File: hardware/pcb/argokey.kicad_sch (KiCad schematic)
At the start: 177 parts, among them J1 USB_BOOT, J2 GPIO, J3 Screen, J4 Debug, J5 USB_C_Receptacle_USB2.0, SW1 RotaryEncoder_Switch, SW2 RESET, U1 W25Q128JVS, U2 RP2040, U3 NCP1117-3.3_SOT223, Y1 ABLS-12.000MHZ-B4-T

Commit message: "Sch: Assign most footprints"
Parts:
- C1, C10, C11, C12, C13, C14, C16, C17, C19, C2, C3, C4, C5, C6, C7, C8, C9: footprint (none) -> Capacitor_SMD:C_0402_1005Metric_Pad0.74x0.62mm_HandSolder
- C15, C18: footprint (none) -> Capacitor_SMD:C_0805_2012Metric_Pad1.18x1.45mm_HandSolder
- D1, D10, D11, D12, D13, D14, D15, D16, D17, D18, D19, D2, D20, D21, D22, D23, D24, D25, D26, D27, D28, D29, D3, D30, D31, D32, D33, D34, D35, D36, D37, D38, D39, D4, D40, D41, D42, D43, D44, D45, D46, D47, D48, D49, D5, D50, D51, D52, D53, D54, D55, D56, D57, D58, D59, D6, D60, D61, D62, D63, D64, D65, D66, D67, D68, D69, D7, D8, D9: footprint (none) -> Diode_SMD:D_SOD-123
- J1: footprint (none) -> Connector_PinHeader_2.54mm:PinHeader_1x02_P2.54mm_Vertical
- J2: footprint (none) -> Connector_PinHeader_2.54mm:PinHeader_1x12_P2.54mm_Horizontal
- J3: footprint (none) -> Connector_PinHeader_2.54mm:PinHeader_1x04_P2.54mm_Vertical
- J4: footprint (none) -> Connector_PinHeader_2.54mm:PinHeader_1x04_P2.54mm_Horizontal
- R1, R10, R2, R3, R4, R5, R6, R7, R8, R9: footprint (none) -> Resistor_SMD:R_0402_1005Metric_Pad0.72x0.64mm_HandSolder
- S1, S10, S11, S12, S14, S15, S16, S17, S19, S20, S21, S22, S24, S25, S26, S27, S29, S30, S31, S32, S33, S34, S35, S36, S37, S38, S39, S40, S41, S42, S43, S44, S45, S46, S47, S48, S49, S5, S50, S51, S52, S53, S54, S55, S56, S58, S59, S6, S60, S62, S63, S66, S67, S68, S7, S8, S9: footprint (none) -> Button_Switch_Keyboard:SW_Cherry_MX_1.00u_PCB
- S13, S18, S23: footprint (none) -> Button_Switch_Keyboard:SW_Cherry_MX_1.25u_PCB
- S2, S65: footprint (none) -> Button_Switch_Keyboard:SW_Cherry_MX_1.50u_PCB
- S28: footprint (none) -> Button_Switch_Keyboard:SW_Cherry_MX_6.25u_PCB
- S3, S57: footprint (none) -> Button_Switch_Keyboard:SW_Cherry_MX_1.75u_PCB
- S4, S61: footprint (none) -> Button_Switch_Keyboard:SW_Cherry_MX_2.25u_PCB
- S64: footprint (none) -> Button_Switch_Keyboard:SW_Cherry_MX_2.00u_PCB
- U2: footprint IC57_RP2040 -> RP2040:RP2040

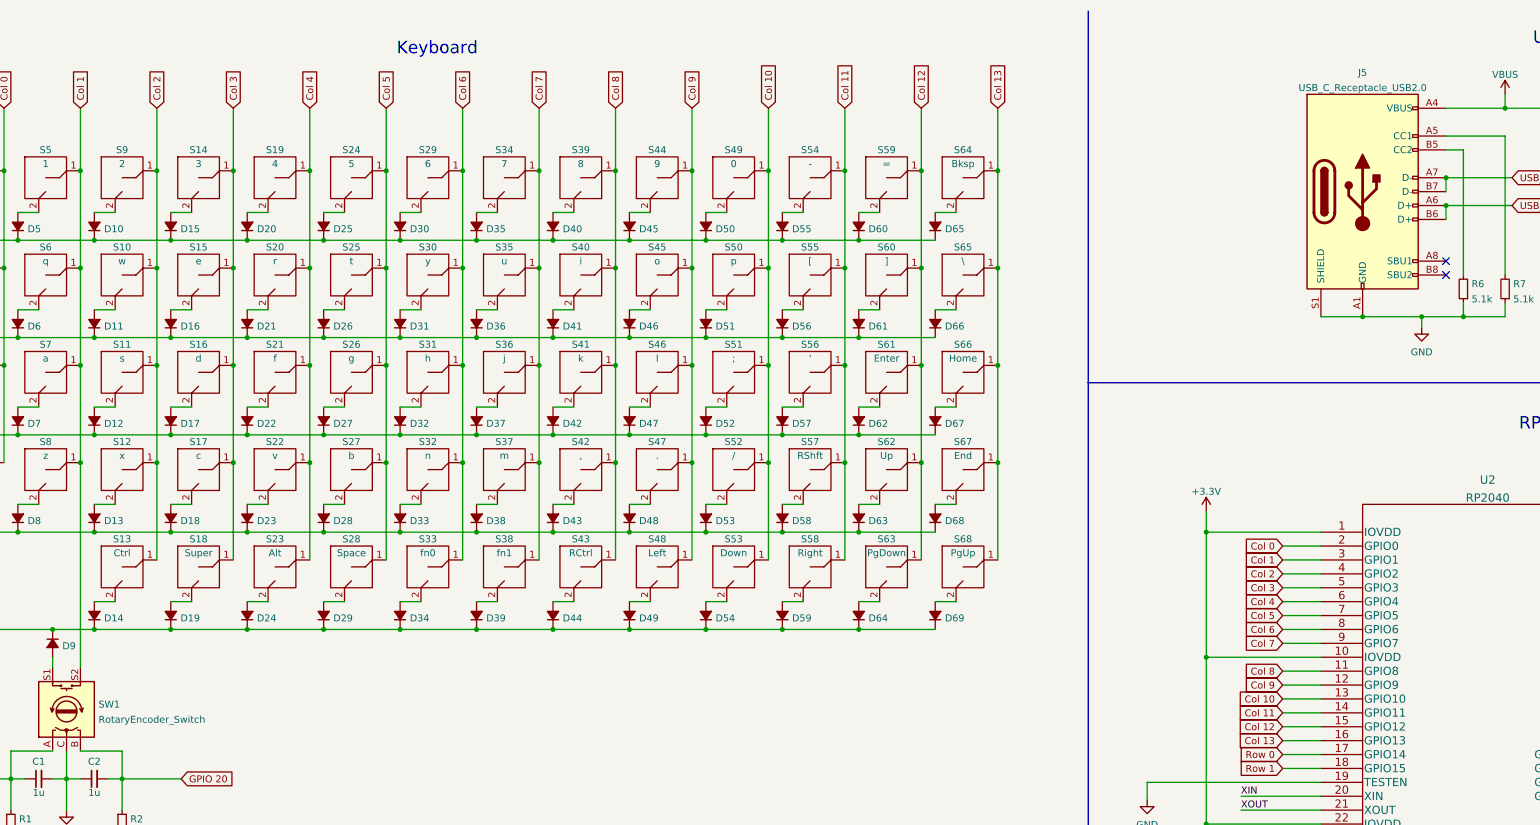
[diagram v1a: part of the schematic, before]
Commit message: Sch: Remove Diode values
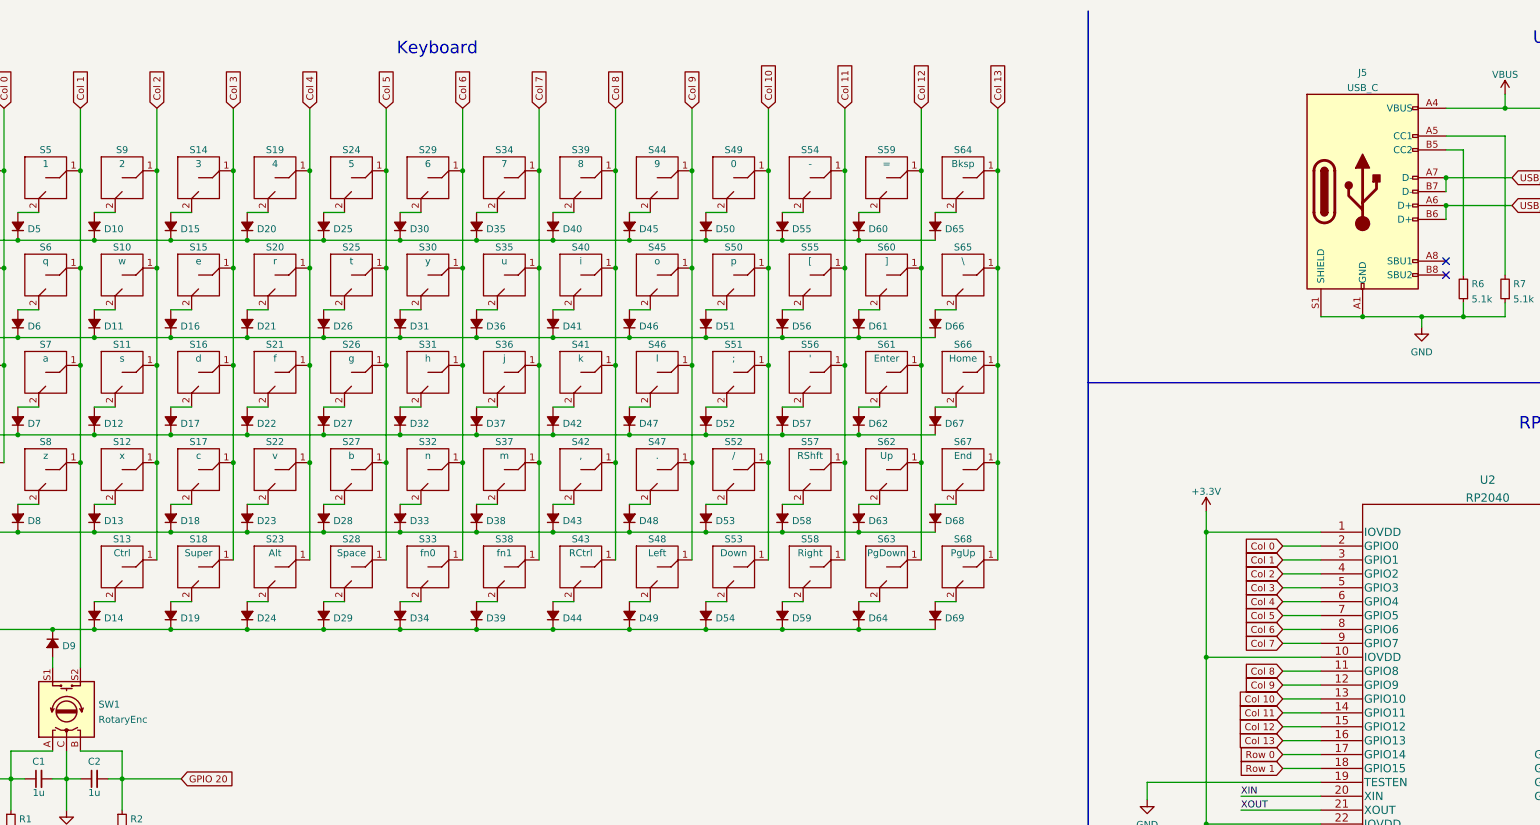
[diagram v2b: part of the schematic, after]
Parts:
- D1, D10, D11, D12, D13, D14, D15, D16, D18, D19, D2, D20, D21, D22, D23, D24, D25, D26, D27, D28, D29, D3, D30, D31, D32, D33, D34, D35, D36, D37, D38, D39, D4, D40, D41, D42, D43, D44, D45, D46, D47, D48, D49, D5, D50, D51, D52, D53, D54, D55, D56, D57, D58, D59, D6, D60, D61, D62, D63, D64, D65, D66, D67, D68, D69, D7, D8, D9: value D_Small_Filled -> ~
- D17: value D_Small_Filled -> (none)
- J5: value USB_C_Receptacle_USB2.0 -> USB_C
- SW1: value RotaryEncoder_Switch -> RotaryEnc

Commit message: PCB: Most traces
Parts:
- J5: footprint (none) -> Connector_USB:USB_C_Receptacle_Amphenol_12401548E4-2A
- SW1: footprint (none) -> Rotary_Encoder:RotaryEncoder_Alps_EC12E-Switch_Vertical_H20mm
- SW2: footprint (none) -> Button_Switch_THT:SW_PUSH_6mm_H4.3mm
- U2: footprint RP2040:RP2040 -> RP2040_minimal:RP2040-QFN-56
- Y1: footprint (none) -> RP2040_minimal:Crystal_SMD_HC49-US
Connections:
- net Col 0: now also SW1.S1
- net Col 1: now also S13.1; no longer SW1.S2
- net Col 2: now also S18.1; no longer S13.1
- net Col 3: now also S23.1; no longer S18.1
- net Col 4: no longer S23.1
- net at D9.2 (A): now also SW1.S2; no longer SW1.S1
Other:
- moved on the sheet: C1, C2, D14, D19, D24, D9, R1, R2, S13, S18, S23, SW1

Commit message: PCB: Most traces
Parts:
- J2: footprint Connector_PinHeader_2.54mm:PinHeader_1x12_P2.54mm_Horizontal -> Connector_PinSocket_2.54mm:PinSocket_1x12_P2.54mm_Horizontal
- J5: footprint Connector_USB:USB_C_Receptacle_Amphenol_12401548E4-2A -> Connector_USB:USB_C_Receptacle_GCT_USB4085
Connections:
- net +3V3: now also J2.2 (Pin_2)
- net Col 0: now also U2.16 (GPIO13); no longer U2.2 (GPIO0)
- net Col 1: now also U2.15 (GPIO12); no longer U2.3 (GPIO1)
- net Col 10: now also U2.5 (GPIO3); no longer U2.13 (GPIO10)
- net Col 11: now also U2.4 (GPIO2); no longer U2.14 (GPIO11)
- net Col 12: now also U2.3 (GPIO1); no longer U2.15 (GPIO12)
- net Col 13: now also U2.2 (GPIO0); no longer U2.16 (GPIO13)
- net Col 2: now also U2.14 (GPIO11); no longer U2.4 (GPIO2)
- net Col 3: now also U2.13 (GPIO10); no longer U2.5 (GPIO3)
- net Col 4: now also U2.12 (GPIO9); no longer U2.6 (GPIO4)
- net Col 5: now also U2.11 (GPIO8); no longer U2.7 (GPIO5)
- net Col 6: now also U2.9 (GPIO7); no longer U2.8 (GPIO6)
- net Col 7: now also U2.8 (GPIO6); no longer U2.9 (GPIO7)
- net Col 8: now also U2.7 (GPIO5); no longer U2.11 (GPIO8)
- net Col 9: now also U2.6 (GPIO4); no longer U2.12 (GPIO9)
- net Row 0: now also U2.29 (GPIO18); no longer U2.17 (GPIO14)
- net Row 1: now also U2.28 (GPIO17); no longer U2.18 (GPIO15)
- net Row 3: now also U2.18 (GPIO15); no longer U2.28 (GPIO17)
- net Row 4: now also U2.17 (GPIO14); no longer U2.29 (GPIO18)
- net SWCLK: now also J4.3 (Pin_3); no longer J4.2 (Pin_2)
- net SWDIO: now also J4.2 (Pin_2); no longer J4.3 (Pin_3)
- net GPIO25 renamed GPIO_25
- net GPIO_19: no longer names the net of U2.30 (GPIO19)
- net GPIO_19: no longer J2.2 (Pin_2)
- no-connect marks 2 -> 3
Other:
- moved on the sheet: C19, R10, R5, R9, SW2, U2

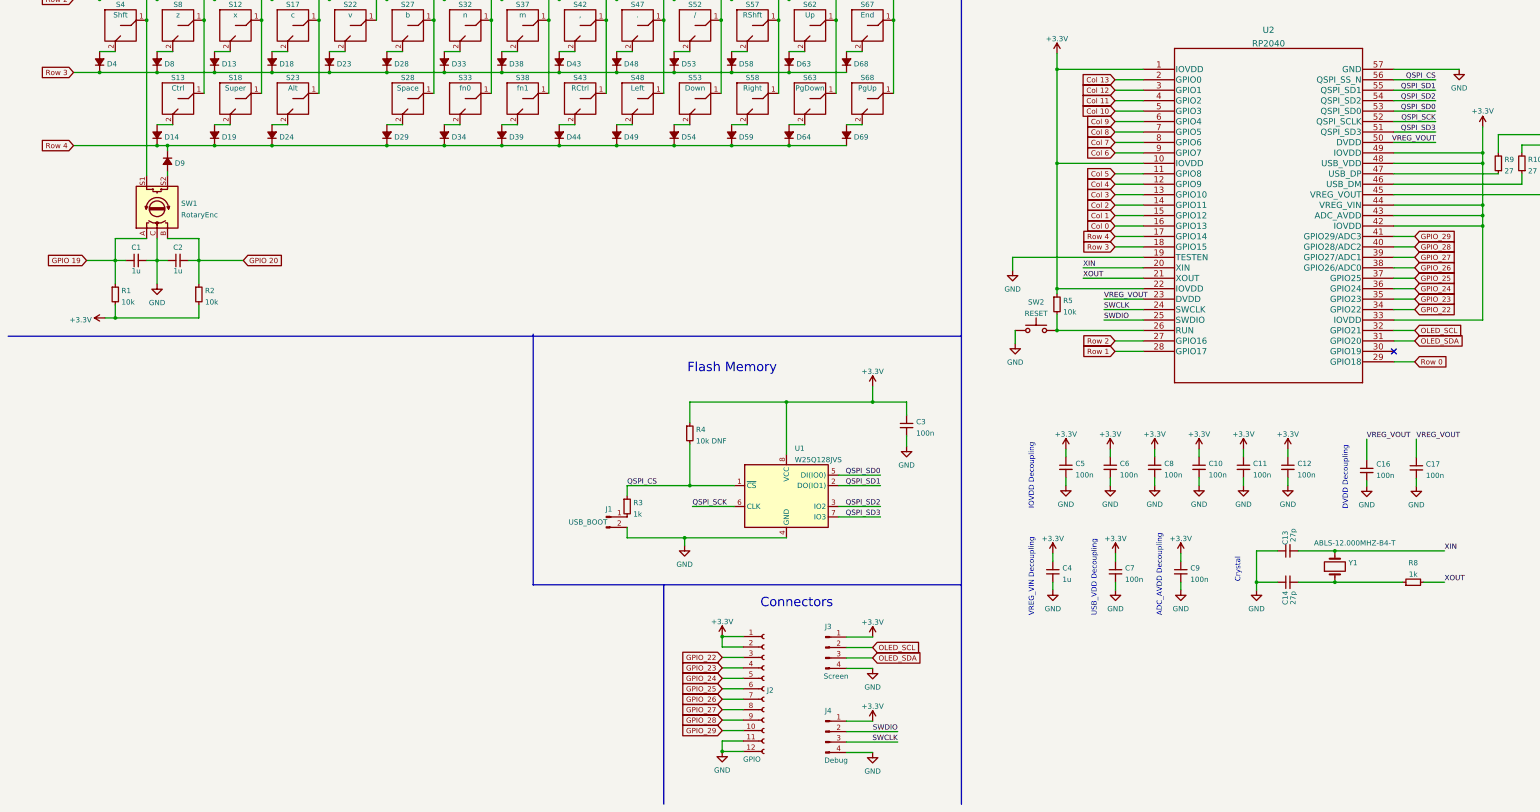
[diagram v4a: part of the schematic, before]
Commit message: Move all smd on one side
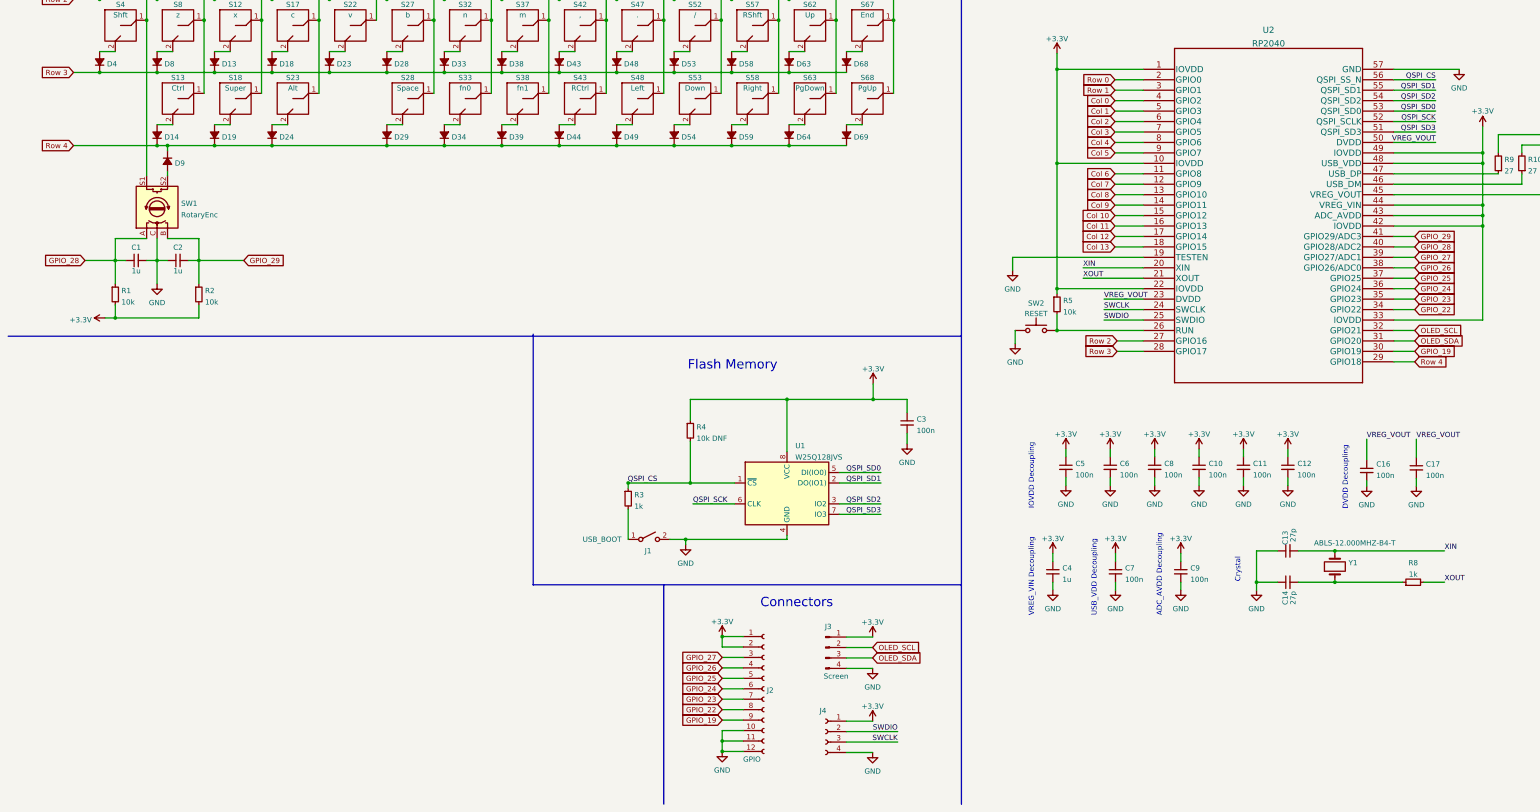
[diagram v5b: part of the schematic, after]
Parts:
- J1: footprint Connector_PinHeader_2.54mm:PinHeader_1x02_P2.54mm_Vertical -> (none); symbol Connector:Conn_01x02_Male -> Switch:SW_SPST
- J4: value Debug -> (none); footprint Connector_PinHeader_2.54mm:PinHeader_1x04_P2.54mm_Horizontal -> (none); symbol Connector:Conn_01x04_Male -> Connector:Conn_01x04_Female
- SW2: footprint Button_Switch_THT:SW_PUSH_6mm_H4.3mm -> (none)
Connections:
- net GPIO 19 is gone; now on net GPIO_28: C1.1, R1.1, SW1.A
- net GPIO 20 is gone; now on net GPIO_29: C2.2, R2.1, SW1.B
- net Col 0: now also U2.4 (GPIO2); no longer U2.16 (GPIO13)
- net Col 1: now also U2.5 (GPIO3); no longer U2.15 (GPIO12)
- net Col 10: now also U2.15 (GPIO12); no longer U2.5 (GPIO3)
- net Col 11: now also U2.16 (GPIO13); no longer U2.4 (GPIO2)
- net Col 12: now also U2.17 (GPIO14); no longer U2.3 (GPIO1)
- net Col 13: now also U2.18 (GPIO15); no longer U2.2 (GPIO0)
- net Col 2: now also U2.6 (GPIO4); no longer U2.14 (GPIO11)
- net Col 3: now also U2.7 (GPIO5); no longer U2.13 (GPIO10)
- net Col 4: now also U2.8 (GPIO6); no longer U2.12 (GPIO9)
- net Col 5: now also U2.9 (GPIO7); no longer U2.11 (GPIO8)
- net Col 6: now also U2.11 (GPIO8); no longer U2.9 (GPIO7)
- net Col 7: now also U2.12 (GPIO9); no longer U2.8 (GPIO6)
- net Col 8: now also U2.13 (GPIO10); no longer U2.7 (GPIO5)
- net Col 9: now also U2.14 (GPIO11); no longer U2.6 (GPIO4)
- net GND: now also J2.10 (Pin_10)
- net GPIO_22: now also J2.8 (Pin_8); no longer J2.3 (Pin_3)
- net GPIO_23: now also J2.7 (Pin_7); no longer J2.4 (Pin_4)
- net GPIO_24: now also J2.6 (Pin_6); no longer J2.5 (Pin_5)
- net GPIO_25: now also J2.5 (Pin_5); no longer J2.6 (Pin_6)
- net GPIO_26: now also J2.4 (Pin_4); no longer J2.7 (Pin_7)
- net GPIO_27: now also J2.3 (Pin_3); no longer J2.8 (Pin_8)
- net GPIO_28: no longer J2.9 (Pin_9)
- net GPIO_29: no longer J2.10 (Pin_10)
- net Row 0: now also U2.2 (GPIO0); no longer U2.29 (GPIO18)
- net Row 1: now also U2.3 (GPIO1); no longer U2.28 (GPIO17)
- net Row 3: now also U2.28 (GPIO17); no longer U2.18 (GPIO15)
- net Row 4: now also U2.29 (GPIO18); no longer U2.17 (GPIO14)
- net GPIO_19: now reaches U2.30 (GPIO19)
- net GPIO_19: now also J2.9 (Pin_9)
- no-connect marks 3 -> 2
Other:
- moved on the sheet: C3, R3, R4, U1

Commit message: Cleanup
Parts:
- J1: footprint (none) -> Button_Switch_SMD:SW_SPDT_PCM12
- J4: value (none) -> Debug; footprint (none) -> Connector_PinSocket_2.54mm:PinSocket_1x04_P2.54mm_Horizontal
- SW2: footprint (none) -> Button_Switch_THT:SW_Tactile_SPST_Angled_PTS645Vx83-2LFS
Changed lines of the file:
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@@
     (property "Reference" "SW2" (id 0) (at 262.001 163.3052 0))
     (property "Value" "RESET" (id 1) (at 262.001 165.8421 0))
-    (property "Footprint" "" (id 2) (at 262.001 164.846 0)
+    (property "Footprint" "Button_Switch_THT:SW_Tactile_SPST_Angled_PTS645Vx83-2LFS" (id 2) (at 262.001 164.846 0)
       (effects (font (size 1.27 1.27)) hide)
     )
@@
     (in_bom yes) (on_board yes)
     (property "Reference" "J4" (id 0) (at 210.185 262.382 0))
-    (property "Value" "" (id 1) (at 208.28 274.447 0))
-    (property "Footprint" "" (id 2) (at 210.82 267.462 0)
+    (property "Value" "Debug" (id 1) (at 208.28 274.447 0))
+    (property "Footprint" "Connector_PinSocket_2.54mm:PinSocket_1x04_P2.54mm_Horizontal" (id 2) (at 210.82 267.462 0)
       (effects (font (size 1.27 1.27)) hide)
     )
@@
     (property "Reference" "J1" (id 0) (at 167.64 223.52 0))
     (property "Value" "USB_BOOT" (id 1) (at 156.464 220.726 0))
-    (property "Footprint" "" (id 2) (at 167.894 220.726 0)
-      (effects (font (size 1.27 1.27)) hide)
-    )
+    (property "Footprint" "Button_Switch_SMD:SW_SPDT_PCM12" (id 2) (at 167.894 220.726 0)
+      (effects (font (size 1.27 1.27)) hide)
+    )

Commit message: First prod rev
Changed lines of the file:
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@@
   (junction (at 185.42 58.928) (diameter 0) (color 0 0 0 0)
-  )
-  (junction (at 185.674 272.288) (diameter 0) (color 0 0 0 0)
   )
   (junction (at 62.23 89.408) (diameter 0) (color 0 0 0 0)
@@
     (stroke (width 0) (type default) (color 0 0 0 0))
   )
-  (polyline (pts (xy 171.45 231.775) (xy 171.45 285.115))
-    (stroke (width 0) (type default) (color 0 0 0 0))
-  )
+  (polyline (pts (xy 139.7 231.902) (xy 139.7 285.242))
+    (stroke (width 0) (type default) (color 0 0 0 0))
+  )
